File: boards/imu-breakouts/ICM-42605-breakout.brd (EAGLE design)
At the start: 15.2 x 12.7 mm, 5 parts, among them IC1 MPU-9250

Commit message: ICM-42605
Breakout for ICM-42605
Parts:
- removed IC1: MPU-9250, RoboJackets-Sensors:QFN-24-4MM2
- added U3: ICM-42605, RoboJackets-Sensors:ICM-442605-2530091
- C1: value 10nF -> (none)
- C2, C3: value 0.1uF -> (none)
- moved C1 1.08 mm to (-3.81, 4.32)
- moved C2 1.08 mm to (-0.25, 4.32)
- moved C3 0.76 mm to (3.81, 4.32)
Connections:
- removed net CS: IC1.22
- removed net N$1: C3.1, IC1.10
- net +3.3V: now also C3.1, U3.P$5, U3.P$8; no longer IC1.1, IC1.13, IC1.8
- net CLK: now also U3.P$13; no longer IC1.23
- net GND: now also U3.P$6, U3.P$7; no longer IC1.11, IC1.18, IC1.20
- net INT: now also U3.P$4, U3.P$9; no longer IC1.12
- net MISO: now also U3.P$1; no longer IC1.9
- net MOSI: now also U3.P$14; no longer IC1.24
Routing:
- net N$1: track 13.2 -> 0.00 mm, vias 2 -> 0
- net +3.3V: track 29.6 -> 24.4 mm, vias 2 -> 0
- net INT: track 6.05 -> 10.8 mm, vias 0 -> 2
- net MISO: track 11.1 -> 8.49 mm
- net CLK: track 9.36 -> 7.13 mm
- net MOSI: track 7.30 -> 9.03 mm
- net GND: track 11.5 -> 11.0 mm, vias 4 -> 5
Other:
- board text added: "ICM-42605"
- board text removed: "MPU-9250"

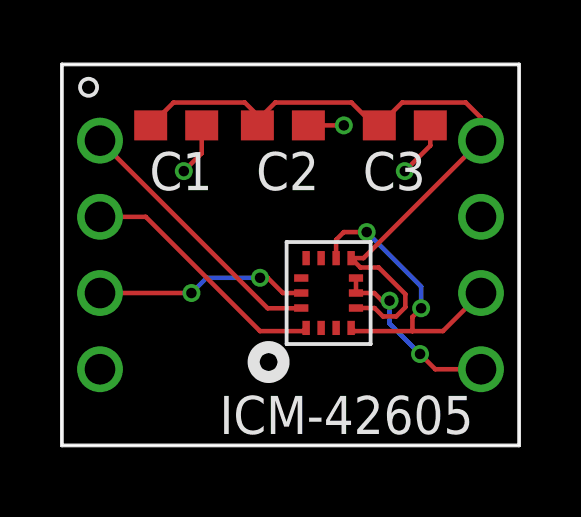
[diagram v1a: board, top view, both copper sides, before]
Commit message: Fixed error in ICM 42605 circuit
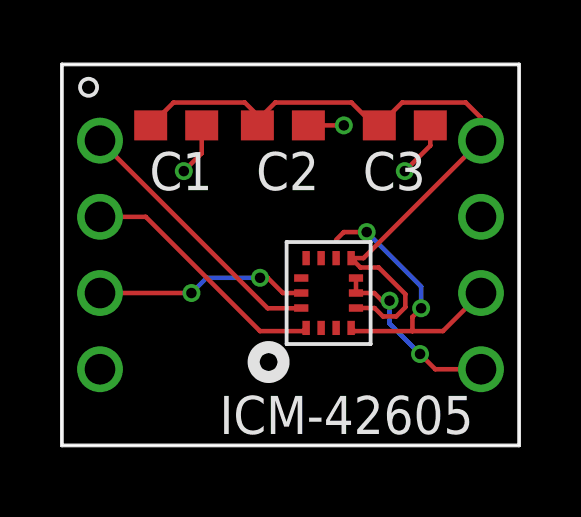
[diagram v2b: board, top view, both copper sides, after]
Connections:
- net !CS!: now also U3.P$12
- net GND: now also U3.P$9
- net INT: no longer U3.P$9
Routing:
- net INT: track 10.8 -> 10.2 mm
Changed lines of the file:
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@@
 <?xml version="1.0" encoding="utf-8"?>
 <!DOCTYPE eagle SYSTEM "eagle.dtd">
-<eagle version="9.5.1">
+<eagle version="9.5.2">
 <drawing>
 <settings>
-<setting alwaysvectorfont="no"/>
+<setting alwaysvectorfont="yes"/>
 <setting verticaltext="up"/>
 </settings>
-<grid distance="10" unitdist="mil" unit="mil" style="lines" multiple="1" display="no" altdistance="5" altunitdist="mil" altunit="mil"/>
+<grid distance="50" unitdist="mil" unit="mil" style="lines" multiple="1" display="yes" altdistance="5" altunitdist="mil" altunit="mil"/>
 <layers>
 <layer number="1" name="Top" color="4" fill="1" visible="yes" active="yes"/>
@@
 <via x="3.81" y="2.794" extent="1-16" drill="0.35"/>
 <wire x1="2.1825" y1="-0.77" x2="2.1825" y2="-1.27" width="0.1524" layer="1"/>
+<contactref element="U3" pad="P$9"/>
+<wire x1="1.778" y1="4.318" x2="3.81" y2="2.794" width="0" layer="19" extent="1-1"/>
+<wire x1="-2.96" y1="4.318" x2="0.596" y2="4.318" width="0" layer="19" extent="1-1"/>
+<wire x1="1.52" y1="-0.1075" x2="3.81" y2="2.794" width="0" layer="19" extent="1-1"/>
+<wire x1="2.1825" y1="-0.77" x2="1.52" y2="-0.1075" width="0" layer="19" extent="1-1"/>
 </signal>
 <signal name="+3.3V">
@@
 <contactref element="KIT1" pad="6"/>
 <contactref element="U3" pad="P$4"/>
-<contactref element="U3" pad="P$9"/>
 <wire x1="6.35" y1="-1.27" x2="5.08" y2="-2.54" width="0.1524" layer="1"/>
 <wire x1="2.1275" y1="-2.54" x2="2.02" y2="-2.4325" width="0.1524" layer="1"/>
 <wire x1="5.08" y1="-2.54" x2="4.064" y2="-2.54" width="0.1524" layer="1"/>
 <wire x1="4.064" y1="-2.54" x2="2.1275" y2="-2.54" width="0.1524" layer="1"/>
-<wire x1="1.52" y1="-0.1075" x2="1.52" y2="0.504" width="0.1524" layer="1"/>
 <wire x1="1.52" y1="0.504" x2="1.778" y2="0.762" width="0.1524" layer="1"/>
 <wire x1="1.778" y1="0.762" x2="2.54" y2="0.762" width="0.1524" layer="1"/>
@@
 <signal name="!CS!">
 <contactref element="KIT1" pad="4"/>
+<contactref element="U3" pad="P$12"/>
+<wire x1="0.3575" y1="-0.77" x2="-6.35" y2="-3.81" width="0" layer="19" extent="1-1"/>
 </signal>
 </signals>

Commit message: Fixed board and text for ICM 42605
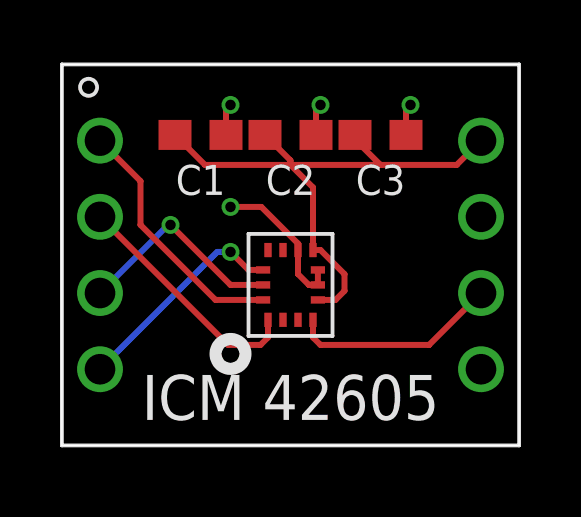
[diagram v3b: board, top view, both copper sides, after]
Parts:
- C1: value (none) -> 0.01uF
- C2: value (none) -> 0.1uF
- C3: value (none) -> 2.2uF
- moved U3 1.30 mm to (0.00, -1.00)
- moved C1 0.87 mm to (-3.00, 4.00)
- moved C3 0.87 mm to (3.00, 4.00)
- moved C2 0.41 mm to (0.00, 4.00)
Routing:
- net !CS!: track 0.00 -> 7.31 mm, vias 0 -> 1
- net +3.3V: track 24.4 -> 19.8 mm
- net INT: track 10.2 -> 7.01 mm, vias 2 -> 0
- net GND: track 11.0 -> 8.27 mm, vias 5 -> 4
- net MOSI: track 9.03 -> 8.49 mm
- net CLK: track 7.13 -> 7.21 mm, vias 2 -> 1
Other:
- board text added: "ICM 42605"
- board text removed: "ICM-42605"

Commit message: Updated breakouts with updated library parts
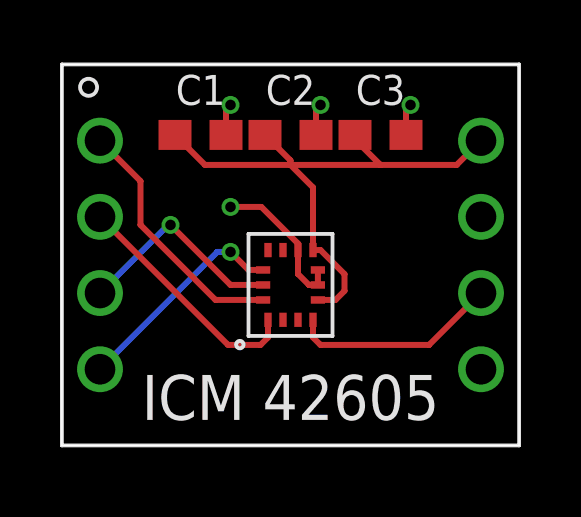
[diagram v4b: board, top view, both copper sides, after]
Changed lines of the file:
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@@
 </element>
 <element name="C3" library="rcl" library_urn="urn:adsk.eagle:library:334" package="C0603" package3d_urn="urn:adsk.eagle:package:23616/2" value="2.2uF" x="3" y="4" smashed="yes">
-<attribute name="NAME" x="3" y="3" size="1" layer="25" font="vector" ratio="15" align="top-center"/>
+<attribute name="NAME" x="3" y="5" size="1" layer="25" font="vector" ratio="15" align="bottom-center"/>
 <attribute name="POPULARITY" value="37" x="3" y="4" size="1.778" layer="27" display="off"/>
 <attribute name="SPICEPREFIX" value="C" x="3" y="4" size="1.778" layer="27" display="off"/>
 </element>
 <element name="C2" library="rcl" library_urn="urn:adsk.eagle:library:334" package="C0603" package3d_urn="urn:adsk.eagle:package:23616/2" value="0.1uF" x="0" y="4" smashed="yes">
-<attribute name="NAME" x="0" y="3" size="1" layer="25" font="vector" ratio="15" align="top-center"/>
+<attribute name="NAME" x="0" y="5" size="1" layer="25" font="vector" ratio="15" align="bottom-center"/>
 <attribute name="POPULARITY" value="37" x="0" y="4" size="1.778" layer="27" display="off"/>
 <attribute name="SPICEPREFIX" value="C" x="0" y="4" size="1.778" layer="27" display="off"/>
 </element>
 <element name="C1" library="rcl" library_urn="urn:adsk.eagle:library:334" package="C0603" package3d_urn="urn:adsk.eagle:package:23616/2" value="0.01uF" x="-3" y="4" smashed="yes">
-<attribute name="NAME" x="-3" y="3" size="1" layer="25" ratio="15" align="top-center"/>
+<attribute name="NAME" x="-3" y="5" size="1" layer="25" ratio="15" align="bottom-center"/>
 <attribute name="POPULARITY" value="37" x="-3" y="4" size="1.778" layer="27" display="off"/>
 <attribute name="SPICEPREFIX" value="C" x="-3" y="4" size="1.778" layer="27" display="off"/>
